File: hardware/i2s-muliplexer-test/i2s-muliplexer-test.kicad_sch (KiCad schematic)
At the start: 21 parts, among them SW1 SW_DIP_x05, SW2 SW_Push_Dual, U2 74HC244, U4 74HC126, U5 74LS138

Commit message: Test circuit can route i2s signals
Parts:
- removed R12: 10k, symbol Device:R_Small
- removed R6: 10K, Resistor_SMD:R_0805_2012Metric_Pad1.15x1.40mm_HandSolder, symbol Device:R_Small
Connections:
- net GND: no longer U2.19 (2OE), U5.15 (O0)
- net CH_EN_2: no longer names the net of U5.13 (O2)
- net CH_EN_3: no longer names the net of U5.12 (O3)
- net CH_EN_4: no longer names the net of U5.11 (O4)
- net CH_EN_5: no longer names the net of U5.10 (O5)
- new net CH_EN_0: U2.19 (2OE), U5.15 (O0)
- no-connect marks 8 -> 12
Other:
- note removed: "CHANGE"
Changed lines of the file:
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@@
   (junction (at 24.13 41.91) (diameter 0) (color 0 0 0 0)
   )
-  (junction (at 181.61 130.81) (diameter 0) (color 0 0 0 0)
-  )
   (junction (at 129.54 133.35) (diameter 0) (color 0 0 0 0)
   )
@@
   )
   (no_connect (at 66.04 107.95))
+  (no_connect (at 66.04 100.33))
+  (no_connect (at 66.04 97.79))
+  (no_connect (at 66.04 95.25))
+  (no_connect (at 66.04 102.87))
   (no_connect (at 91.44 50.8))
   (no_connect (at 101.6 50.8))
@@
     (stroke (width 0) (type default) (color 0 0 0 0))
   )
-  (wire (pts (xy 57.15 180.34) (xy 46.99 180.34))
-    (stroke (width 0) (type default) (color 255 153 0 1))
-  )
   (wire (pts (xy 132.08 143.51) (xy 129.54 143.51))
     (stroke (width 0) (type default) (color 0 0 0 0))
@@
     (stroke (width 0) (type default) (color 0 0 0 0))
   )
-  (wire (pts (xy 157.48 130.81) (xy 181.61 130.81))
-    (stroke (width 0) (type default) (color 0 0 0 0))
-  )
   (wire (pts (xy 81.28 138.43) (xy 85.09 138.43))
     (stroke (width 0) (type default) (color 0 0 0 0))
@@
     (stroke (width 0) (type default) (color 0 0 0 0))
   )
-  (wire (pts (xy 19.05 177.8) (xy 19.05 175.26))
-    (stroke (width 0) (type default) (color 0 0 0 0))
-  )
   (polyline (pts (xy 43.18 153.67) (xy 40.64 153.67))
     (stroke (width 0) (type default) (color 0 0 0 0))
@@
     (stroke (width 0) (type default) (color 0 0 0 0))
   )
-  (wire (pts (xy 19.05 171.45) (xy 19.05 170.18))
-    (stroke (width 0) (type default) (color 0 0 0 0))
-  )
   (wire (pts (xy 45.72 39.37) (xy 68.58 39.37))
     (stroke (width 0) (type default) (color 0 0 0 0))
@@
     (stroke (width 0) (type default) (color 0 0 0 0))
   )
+  (wire (pts (xy 46.99 177.8) (xy 57.15 177.8))
+    (stroke (width 0) (type default) (color 0 0 0 0))
+  )
   (bus (pts (xy 97.79 74.93) (xy 97.79 81.28))
     (stroke (width 0) (type default) (color 0 0 0 0))
   )
+  (wire (pts (xy 46.99 180.34) (xy 57.15 180.34))
+    (stroke (width 0) (type default) (color 0 0 0 0))
+  )
   (wire (pts (xy 129.54 120.65) (xy 129.54 133.35))
     (stroke (width 0) (type default) (color 0 0 0 0))
   )
-  (wire (pts (xy 66.04 97.79) (xy 77.47 97.79))
-    (stroke (width 0) (type default) (color 0 0 0 0))
-  )
   (wire (pts (xy 132.08 146.05) (xy 100.33 146.05))
     (stroke (width 0) (type default) (color 0 0 0 0))
@@
     (stroke (width 0) (type default) (color 0 0 0 0))
   )
-  (wire (pts (xy 181.61 130.81) (xy 185.42 130.81))
-    (stroke (width 0) (type default) (color 0 0 0 0))
-  )
-  (wire (pts (xy 66.04 102.87) (xy 77.47 102.87))
+  (wire (pts (xy 157.48 130.81) (xy 185.42 130.81))
     (stroke (width 0) (type default) (color 0 0 0 0))
   )
@@
     (stroke (width 0) (type default) (color 0 0 0 0))
   )
-  (wire (pts (xy 19.05 177.8) (xy 57.15 177.8))
-    (stroke (width 0) (type default) (color 255 153 0 1))
-  )
   (polyline (pts (xy 40.64 153.67) (xy 40.64 163.83))
     (stroke (width 0) (type default) (color 0 0 0 0))
@@
     (stroke (width 0) (type default) (color 0 0 0 0))
   )
-  (wire (pts (xy 66.04 100.33) (xy 77.47 100.33))
-    (stroke (width 0) (type default) (color 0 0 0 0))
-  )
   (wire (pts (xy 24.13 41.91) (xy 24.13 44.45))
     (stroke (width 0) (type default) (color 0 0 0 0))
@@
   )
   (wire (pts (xy 132.08 133.35) (xy 129.54 133.35))
-    (stroke (width 0) (type default) (color 0 0 0 0))
-  )
-  (wire (pts (xy 66.04 95.25) (xy 77.47 95.25))
     (stroke (width 0) (type default) (color 0 0 0 0))
   )
@@
     (effects (font (size 1.27 1.27) bold) (justify left bottom))
   )
-  (text "CHANGE" (at 36.83 181.61 0)
-    (effects (font (size 1.27 1.27) bold italic) (justify left bottom))
-  )
   (text "100R input resistors?" (at 36.83 135.89 0)
     (effects (font (size 1.27 1.27)) (justify left bottom))
@@
     (effects (font (size 1.27 1.27)) (justify left bottom))
   )
-  (label "CH_EN_4" (at 68.58 100.33 0)
-    (effects (font (size 1.27 1.27)) (justify left bottom))
-  )
-  (label "CH_EN_5" (at 68.58 102.87 0)
-    (effects (font (size 1.27 1.27)) (justify left bottom))
-  )
   (label "BCLK" (at 82.55 167.64 0)
     (effects (font (size 1.27 1.27)) (justify left bottom))
@@
     (effects (font (size 1.27 1.27)) (justify right bottom))
   )
-  (label "CH_EN_3" (at 68.58 97.79 0)
-    (effects (font (size 1.27 1.27)) (justify left bottom))
-  )
   (label "DATA" (at 82.55 160.02 0)
     (effects (font (size 1.27 1.27)) (justify left bottom))
@@
   (label "BCLK" (at 107.95 146.05 180)
     (effects (font (size 1.27 1.27)) (justify right bottom))
-  )
-  (label "CH_EN_2" (at 68.58 95.25 0)
-    (effects (font (size 1.27 1.27)) (justify left bottom))
   )
   (label "MCLK" (at 82.55 162.56 0)
@@
     )
     (property "Datasheet" "" (id 3) (at 69.85 147.32 0)
-      (effects (font (size 1.27 1.27)) hide)
-    )
-    (pin "1")
-  )
-  (symbol (lib_id "Device:R_Small") (at 181.61 133.35 0) (unit 1)
-    (in_bom yes) (on_board yes)
-    (property "Reference" "R6" (id 0) (at 183.1086 132.1816 0)
-      (effects (font (size 1.27 1.27)) (justify left))
-    )
-    (property "Value" "10K" (id 1) (at 183.1086 134.493 0)
-      (effects (font (size 1.27 1.27)) (justify left))
-    )
-    (property "Footprint" "Resistor_SMD:R_0805_2012Metric_Pad1.15x1.40mm_HandSolder" (id 2) (at 181.61 133.35 0)
-      (effects (font (size 1.27 1.27)) hide)
-    )
-    (property "Datasheet" "~" (id 3) (at 181.61 133.35 0)
-      (effects (font (size 1.27 1.27)) hide)
-    )
-    (pin "1")
-    (pin "2")
-  )
-  (symbol (lib_id "power:GND") (at 46.99 180.34 0) (unit 1)
-    (in_bom yes) (on_board yes)
-    (property "Reference" "#PWR06" (id 0) (at 46.99 186.69 0)
-      (effects (font (size 1.27 1.27)) hide)
-    )
-    (property "Value" "GND" (id 1) (at 46.99 184.15 0))
-    (property "Footprint" "" (id 2) (at 46.99 180.34 0)
-      (effects (font (size 1.27 1.27)) hide)
-    )
-    (property "Datasheet" "" (id 3) (at 46.99 180.34 0)
       (effects (font (size 1.27 1.27)) hide)
     )
@@
     (pin "8")
     (pin "9")
-  )
-  (symbol (lib_id "power:+3V3") (at 19.05 171.45 0) (unit 1)
-    (in_bom yes) (on_board yes) (fields_autoplaced)
-    (property "Reference" "#PWR05" (id 0) (at 19.05 175.26 0)
-      (effects (font (size 1.27 1.27)) hide)
-    )
-    (property "Value" "+3V3" (id 1) (at 19.05 167.8742 0))
-    (property "Footprint" "" (id 2) (at 19.05 171.45 0)
-      (effects (font (size 1.27 1.27)) hide)
-    )
-    (property "Datasheet" "" (id 3) (at 19.05 171.45 0)
-      (effects (font (size 1.27 1.27)) hide)
-    )
-    (pin "1")
-  )
-  (symbol (lib_id "power:GND") (at 181.61 135.89 0) (unit 1)
-    (in_bom yes) (on_board yes)
-    (property "Reference" "#PWR026" (id 0) (at 181.61 142.24 0)
-      (effects (font (size 1.27 1.27)) hide)
-    )
-    (property "Value" "GND" (id 1) (at 181.737 140.2842 0))
-    (property "Footprint" "" (id 2) (at 181.61 135.89 0)
-      (effects (font (size 1.27 1.27)) hide)
-    )
-    (property "Datasheet" "" (id 3) (at 181.61 135.89 0)
-      (effects (font (size 1.27 1.27)) hide)
-    )
-    (pin "1")
   )
   (symbol (lib_id "Device:R_Small") (at 105.41 41.91 0) (unit 1)
@@
     (pin "2")
   )
-  (symbol (lib_id "Device:R_Small") (at 19.05 172.72 0) (unit 1)
-    (in_bom yes) (on_board yes) (fields_autoplaced)
-    (property "Reference" "R12" (id 0) (at 20.5486 171.8853 0)
-      (effects (font (size 1.27 1.27)) (justify left))
-    )
-    (property "Value" "10k" (id 1) (at 20.5486 174.4222 0)
-      (effects (font (size 1.27 1.27)) (justify left))
-    )
-    (property "Footprint" "" (id 2) (at 19.05 172.72 0)
-      (effects (font (size 1.27 1.27)) hide)
-    )
-    (property "Datasheet" "~" (id 3) (at 19.05 172.72 0)
-      (effects (font (size 1.27 1.27)) hide)
-    )
-    (pin "1")
-    (pin "2")
-  )
   (symbol (lib_id "power:+3V3") (at 157.48 113.03 0) (unit 1)
     (in_bom yes) (on_board yes)
@@
       (reference "#PWR04") (unit 1) (value "+3V3") (footprint "")
     )
-    (path "/57c00125-3ef1-4c36-bf6c-39354c96a6ad"
-      (reference "#PWR05") (unit 1) (value "+3V3") (footprint "")
-    )
-    (path "/4509af53-43b5-4316-9a9b-37470cf88277"
-      (reference "#PWR06") (unit 1) (value "GND") (footprint "")
-    )
     (path "/36cfb9b4-3553-47ee-9268-dd86eda6299b"
       (reference "#PWR09") (unit 1) (value "+3.3V") (footprint "")
@@
       (reference "#PWR025") (unit 1) (value "GND") (footprint "")
     )
-    (path "/5dc857cd-69b3-436f-ad40-03b225e423ed"
-      (reference "#PWR026") (unit 1) (value "GND") (footprint "")
-    )
     (path "/01fef755-0f7b-4612-854f-9df10a82204d"
       (reference "#PWR027") (unit 1) (value "GND") (footprint "")
@@
       (reference "R5") (unit 1) (value "10K") (footprint "Resistor_SMD:R_0805_2012Metric_Pad1.15x1.40mm_HandSolder")
     )
-    (path "/3c9fcff9-2ccd-404a-8b7d-bbda4f6b62ee"
-      (reference "R6") (unit 1) (value "10K") (footprint "Resistor_SMD:R_0805_2012Metric_Pad1.15x1.40mm_HandSolder")
-    )
     (path "/05cdcb9b-1c23-46c6-91cd-4a8a325e3f0b"
       (reference "R7") (unit 1) (value "10K") (footprint "Resistor_SMD:R_0805_2012Metric_Pad1.15x1.40mm_HandSolder")
@@
       (reference "R11") (unit 1) (value "10K") (footprint "Resistor_SMD:R_0805_2012Metric_Pad1.15x1.40mm_HandSolder")
     )
-    (path "/e36a30f8-c8f4-41e5-b6c3-f833645e2caa"
-      (reference "R12") (unit 1) (value "10k") (footprint "")
-    )
     (path "/537de23f-0953-4910-9e05-9c3b7a46f9bb"

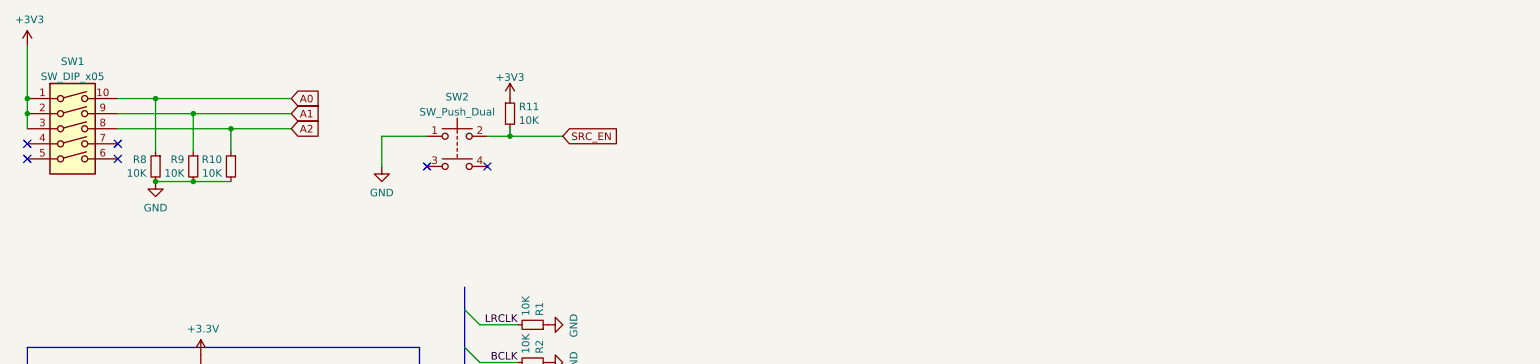
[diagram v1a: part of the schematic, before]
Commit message: Added i2s multiplexer test code
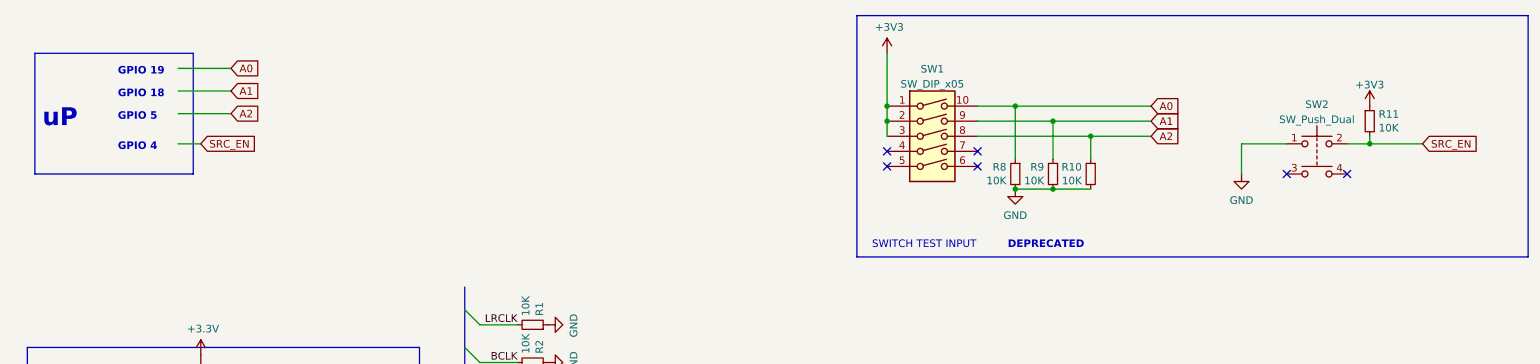
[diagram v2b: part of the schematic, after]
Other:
- note added: "DEPRECATED"
- note added: "GPIO 18"
- note added: "GPIO 19"
- note added: "GPIO 4"
- note added: "GPIO 5"
- note added: "SWITCH TEST INPUT"
- note added: "uP"
- moved on the sheet: R10, R11, R8, R9, SW1, SW2
